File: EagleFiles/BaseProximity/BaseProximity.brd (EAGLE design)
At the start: 99.1 x 79.2 mm, 30 parts

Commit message: v1 of proximity board completed
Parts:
- removed JP1: (no value), pinhead:1X02
- moved LED1 35.3 mm to (54.6, 38.1), turned to 90 degrees
- moved R11 23.3 mm to (50.8, 38.1), turned to 0 degrees
- moved D1 9.67 mm to (80.0, 48.3), turned to 270 degrees
- moved D3 7.95 mm to (80.0, 57.1), turned to 270 degrees
- moved R6 7.82 mm to (78.7, 54.6)
- moved R1 5.68 mm to (78.7, 50.8), turned to 270 degrees
- moved JP7 3.59 mm to (87.6, 55.9), turned to 0 degrees
- moved D2 3.59 mm to (63.5, 43.2)
- moved C13 2.25 mm to (64.8, 61.0), turned to 0 degrees
- moved R2 1.80 mm to (67.3, 43.2)
- moved 5983 1.27 mm to (66.0, 71.1)
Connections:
- removed net VIN: JP1.1
- net +5V: now also LED1.A
- net GND: no longer JP1.2
- net VCC: no longer LED1.A
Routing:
- net VCC: track 347.2 -> 456.8 mm, vias 0 -> 4
- net +5V: track 15.2 -> 94.5 mm, vias 0 -> 3
- net SCL: track 52.5 -> 105.4 mm, vias 0 -> 1
- net SDA: track 48.6 -> 91.5 mm, vias 0 -> 1
- net GPIO18: track 47.8 -> 83.7 mm
- net RX-RSP: track 0.00 -> 22.3 mm, vias 0 -> 1
- net GPIO23: track 31.3 -> 52.6 mm
- net TX-RSP: track 0.00 -> 15.6 mm, vias 0 -> 1
- net GPIO20: track 89.4 -> 96.9 mm
- net GPIO22: track 0.00 -> 2.96 mm
- net N$4: track 0.00 -> 2.08 mm
- net N$2: track 0.00 -> 2.08 mm
- net N$1: track 0.00 -> 1.85 mm
- net N$7: track 0.00 -> 1.85 mm
- net GND: track 1.24 -> 0.00 mm, vias 2 -> 0

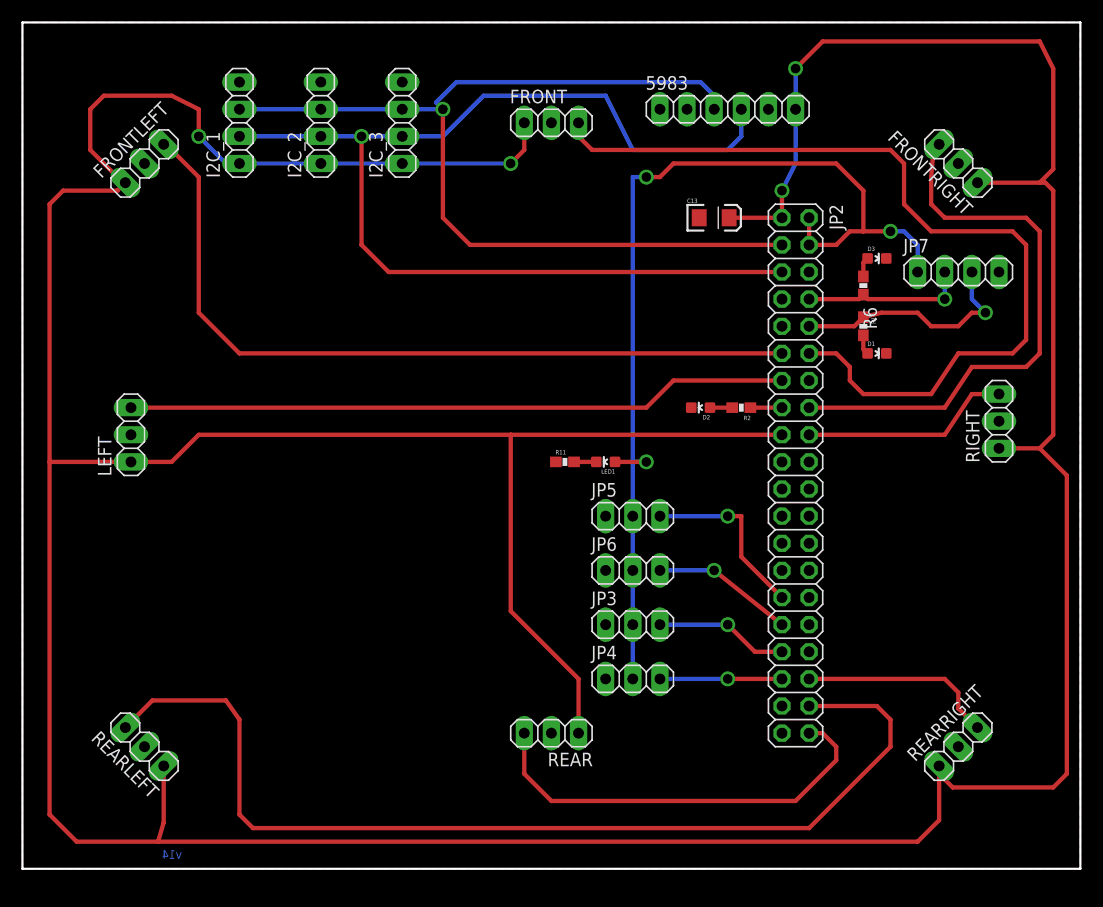
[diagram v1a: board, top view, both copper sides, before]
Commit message: add shopping list and getting started
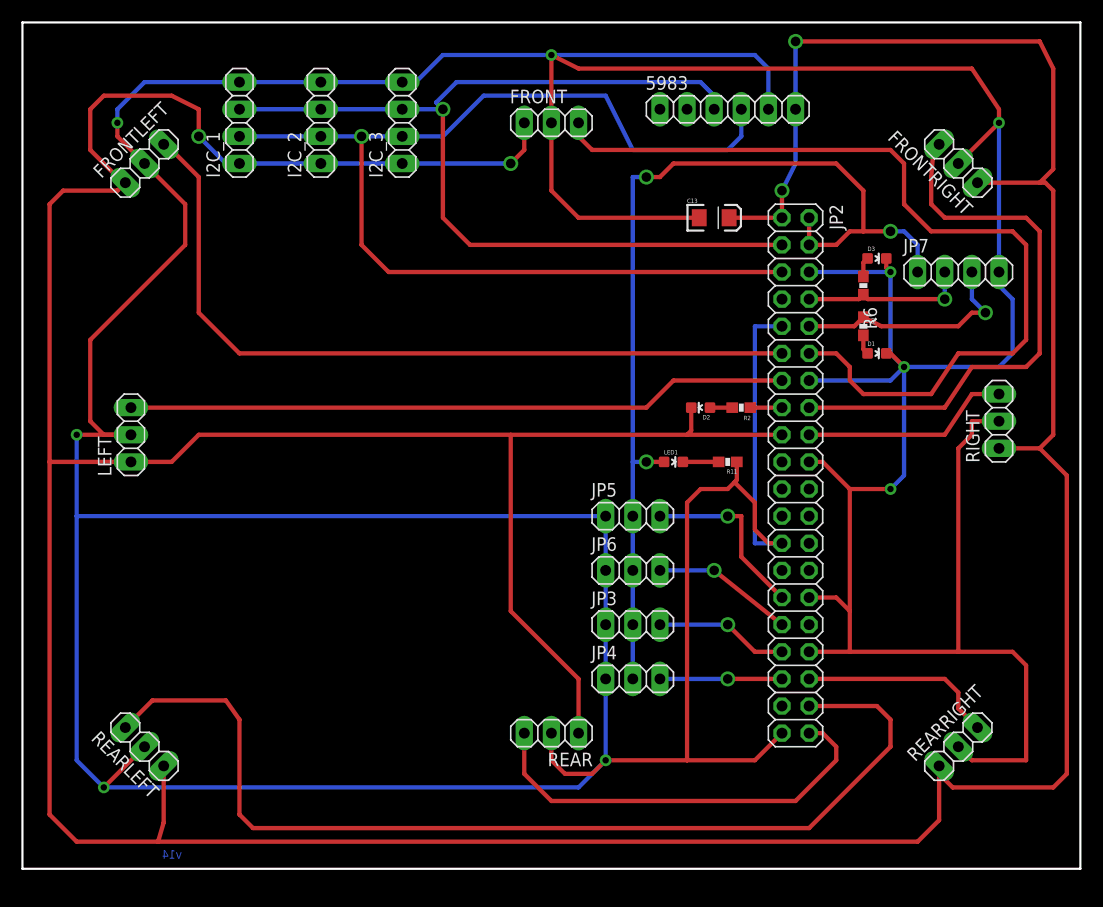
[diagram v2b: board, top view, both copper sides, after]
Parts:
- moved R11 15.2 mm to (66.0, 38.1), turned to 180 degrees
- moved LED1 6.35 mm to (61.0, 38.1), turned to 270 degrees
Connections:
- net GND: no longer D2.C
- net VCC: now also D2.C
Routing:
- net GND: track 0.00 -> 606.4 mm, vias 0 -> 9
- net VCC: track 456.8 -> 461.0 mm
- net +5V: track 94.5 -> 93.2 mm
- net N$4: track 2.08 -> 3.35 mm
- removed copper zone on layer 1, net GND
- removed copper zone on layer 16, net GND

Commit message: updated dox, and stubs for controlling with XBox Controller
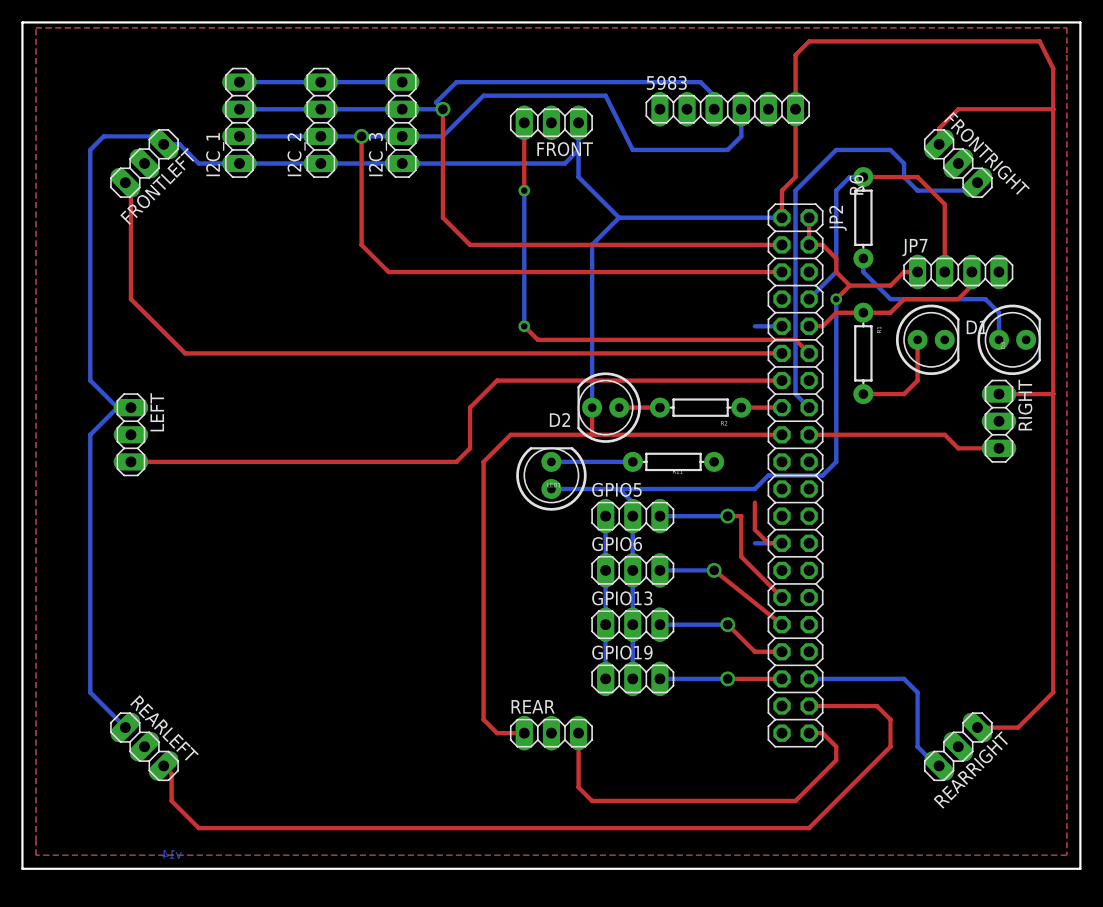
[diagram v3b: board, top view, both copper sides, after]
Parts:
- removed C13: 10uF, SparkFun:EIA3216
- D1, D2, D3, LED1: device Testing:0603-LED-ALT1 -> SparkFun-LED:LED5MM
- R1, R2, R6: value 330 -> 1K; device SparkFun:0603-RES -> SparkFun-Resistors:AXIAL-0.3
- R11: value 10K -> 1K; device SparkFun:0603-RES -> SparkFun-Resistors:AXIAL-0.3
- moved D3 14.8 mm to (92.7, 49.5), turned to 0 degrees
- moved LED1 11.5 mm to (49.5, 36.8), turned to 90 degrees
- moved D2 8.89 mm to (54.6, 43.2), turned to 180 degrees
- moved R6 6.35 mm to (78.7, 61.0), turned to 270 degrees
- moved D1 5.24 mm to (85.1, 49.5), turned to 0 degrees
- moved R11 5.08 mm to (61.0, 38.1)
- moved R2 3.81 mm to (63.5, 43.2)
- moved R1 2.54 mm to (78.7, 48.3)
- turned FRONT to 180 degrees
- turned FRONTLEFT to 225 degrees
- turned FRONTRIGHT to 315 degrees
- turned LEFT to 270 degrees
- turned REAR to 0 degrees
- turned REARLEFT to 315 degrees
- turned REARRIGHT to 225 degrees
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- renumbered JP3 to GPIO13, JP4 to GPIO19, JP5 to GPIO5, JP6 to GPIO6
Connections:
- net GND: now also D1.K, D3.K, R11.P$1; no longer C13.C, D1.C, D3.C, R11.1
- net GPIO22: now also R2.P$1; no longer R2.1
- net N$1: now also R1.P$2; no longer R1.2
- net N$2: now also R2.P$2; no longer R2.2
- net N$4: now also LED1.K, R11.P$2; no longer LED1.C, R11.2
- net N$7: now also R6.P$2; no longer R6.2
- net RX-RSP: now also R1.P$1; no longer R1.1
- net TX-RSP: now also R6.P$1; no longer R6.1
- net VCC: now also D2.K; no longer C13.A, D2.C
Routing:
- net GND: track 606.4 -> 41.2 mm, vias 9 -> 0
- net VCC: track 461.0 -> 338.2 mm, vias 4 -> 0
- net GPIO18: track 83.7 -> 46.8 mm, vias 0 -> 2
- net N$7: track 1.85 -> 18.1 mm
- net +5V: track 93.2 -> 78.6 mm, vias 3 -> 1
- net TX-RSP: track 15.6 -> 29.3 mm, vias 1 -> 0
- net GPIO20: track 96.9 -> 85.8 mm
- net GPIO23: track 52.6 -> 42.1 mm
- net N$1: track 1.85 -> 9.42 mm
- net GPIO27: track 62.0 -> 66.3 mm
- net GPIO21: track 40.0 -> 35.7 mm
- net N$4: track 3.35 -> 7.62 mm
- net RX-RSP: track 21.9 -> 18.1 mm, vias 1 -> 0
- net N$2: track 2.08 -> 3.81 mm
- net GPIO24: track 19.8 -> 18.3 mm
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- added copper zone on layer 1, net GND
- added copper zone on layer 16, net GND

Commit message: board design w/ switch IR
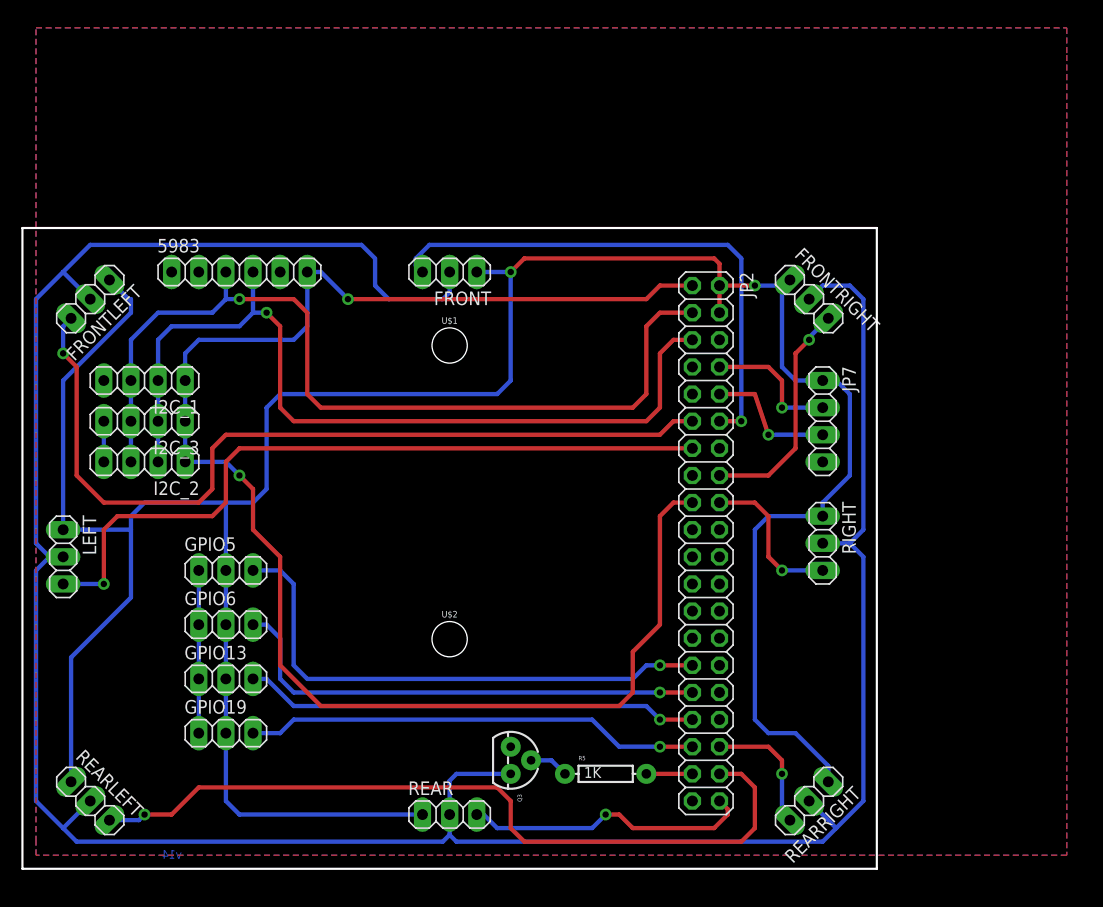
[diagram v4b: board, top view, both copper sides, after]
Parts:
- removed D1, D2, D3: Green, SparkFun-LED:LED5MM
- removed LED1: Red, SparkFun-LED:LED5MM
- removed R1, R11, R2, R6: 1K, SparkFun-Resistors:AXIAL-0.3
- added Q3: 2N3904, SparkFun-DiscreteSemi:TO-92-EZ
- added R5: 1K, SparkFun-Resistors:AXIAL-0.3EZ
- added U$1, U$2: (no value), SparkFun-Hardware:STAND-OFF
- moved 5983 48.2 mm to (20.3, 55.9)
- moved GPIO19 38.4 mm to (19.1, 12.7)
- moved GPIO5 38.4 mm to (19.1, 27.9)
- moved GPIO6 38.4 mm to (19.1, 22.9)
- moved GPIO13 38.4 mm to (19.1, 17.8)
- moved I2C_3 36.9 mm to (11.4, 41.9), turned to 180 degrees
- moved I2C_2 35.8 mm to (11.4, 38.1), turned to 180 degrees
- moved I2C_1 25.7 mm to (11.4, 45.7), turned to 180 degrees
- moved RIGHT 20.1 mm to (74.9, 30.5)
- moved FRONTRIGHT 18.9 mm to (73.7, 53.3)
- moved JP7 18.9 mm to (74.9, 41.9), turned to 270 degrees
- moved FRONT 16.9 mm to (40.0, 55.9)
- moved REARRIGHT 14.9 mm to (73.7, 6.35)
- moved FRONTLEFT 13.7 mm to (6.35, 53.3)
- moved LEFT 13.1 mm to (3.81, 29.2)
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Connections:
- removed net N$1: D1.A, R1.P$2
- removed net N$2: D2.A, R2.P$2
- removed net N$4: LED1.K, R11.P$2
- removed net N$7: D3.A, R6.P$2
- new net IR_GND: FRONT.2, FRONTLEFT.2, FRONTRIGHT.2, LEFT.2, Q3.3, REAR.2, REARLEFT.2, REARRIGHT.2, RIGHT.2
- new net N$3: Q3.2, R5.P$1
- net +5V: now also FRONT.1, FRONTLEFT.1, FRONTRIGHT.1, LEFT.1, REAR.1, REARLEFT.1, REARRIGHT.1, RIGHT.1; no longer LED1.A
- net GND: now also Q3.1; no longer D1.K, D3.K, FRONT.2, FRONTLEFT.2, FRONTRIGHT.2, LEFT.2, R11.P$1, REAR.2, REARLEFT.2, REARRIGHT.2, RIGHT.2
- net GPIO22: no longer R2.P$1
- net GPIO26: now also R5.P$2
- net RX-RSP: no longer R1.P$1
- net TX-RSP: no longer R6.P$1
- net VCC: no longer D2.K, FRONT.1, FRONTLEFT.1, FRONTRIGHT.1, LEFT.1, REAR.1, REARLEFT.1, REARRIGHT.1, RIGHT.1
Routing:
- net IR_GND: track 0.00 -> 255.6 mm
- net VCC: track 338.2 -> 146.6 mm, vias 0 -> 2
- net +5V: track 78.6 -> 260.0 mm, vias 1 -> 2
- net GPIO5: track 16.8 -> 50.3 mm
- net GPIO6: track 13.2 -> 46.0 mm
- net GPIO19: track 11.4 -> 42.7 mm
- net GPIO13: track 12.5 -> 42.7 mm
- net SCL: track 105.4 -> 81.1 mm
- net GND: track 41.2 -> 19.0 mm
- net GPIO23: track 42.1 -> 21.6 mm, vias 0 -> 1
- net N$7: track 18.1 -> 0.00 mm
- net TX-RSP: track 29.3 -> 12.7 mm, vias 0 -> 1
- net GPIO20: track 85.8 -> 73.5 mm, vias 0 -> 1
- net N$1: track 9.42 -> 0.00 mm
- net GPIO21: track 35.7 -> 27.2 mm, vias 0 -> 1
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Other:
- board size 99.1 x 79.2 mm -> 80 x 60 mm

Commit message: board order for v1.0
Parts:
- added Q1: 2N3904, SparkFun-DiscreteSemi:TO-92-EZ
- added R1: 1K, SparkFun-Resistors:AXIAL-0.3EZ
- moved Q3 34.3 mm to (11.4, 11.4), turned to 180 degrees
- moved R5 34.3 mm to (20.3, 8.89)
- renumbered 5983 to COMPASS, JP7 to TO_MBOT
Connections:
- new net IR_GND2: FRONTRIGHT.2, Q1.3, REAR.2, REARRIGHT.2, RIGHT.2
- new net N$1: Q1.2, R1.P$1
- net GND: now also Q1.1
- net GPIO12: now also R1.P$2
- net IR_GND: no longer FRONTRIGHT.2, REAR.2, REARRIGHT.2, RIGHT.2
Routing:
- net IR_GND: track 255.6 -> 111.1 mm
- net IR_GND2: track 0.00 -> 107.4 mm
- net GPIO26: track 4.31 -> 38.6 mm
- net GPIO12: track 0.00 -> 13.3 mm
- net N$1: track 0.00 -> 3.70 mm
- net N$3: track 3.70 -> 5.34 mm
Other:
- board text added: "+5V"
- board text added: "GND"
- board text added: "MARCH 2017"
- board text added: "REV1.0"
- board text added: "RX <"
- board text added: "TX >"
- board text added: "Tampa IoT Society"
- board text added: "https://GitHub.com/LaserTankBot"
- board text removed: "v14"
